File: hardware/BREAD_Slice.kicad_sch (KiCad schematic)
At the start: 15 parts, among them J1 I2C_01x04, J2 Conn_01x10_Female

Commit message: added opamps
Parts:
- removed J1: I2C_01x04, Connector_JST:JST_SH_SM04B-SRSS-TB_1x04-1MP_P1.00mm_Horizontal, symbol SparkFun-Connector:I2C_01x04
- added NT1: NetTie_2, NetTie:NetTie-2_SMD_Pad2.0mm, symbol Device:NetTie_2
- added U2: LM339, symbol Comparator:LM339
- added U3: MCP6242T-E/SN, Package_DFN_QFN:DFN-8-1EP_3x2mm_P0.5mm_EP1.75x1.45mm, symbol Amplifier_Operational:MCP6002-xMC
- added U4: TLC27L2BCDR, Package_SO:SOIC-8_3.9x4.9mm_P1.27mm, symbol Amplifier_Operational:TLC27M2xD
- D1: PROD_ID (none) -> DIO-12503
- HS1: footprint KML-Custom:Thermal Pad -> kml-custom:Thermal Pad
- U1: value ~ -> AP63205
- renumbered J2 to J1
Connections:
- net GND: now also NT1.1; no longer J1.1 (Pin_1), J1.10 (Pin_10), J1.5 (Pin_5)
- net E_STOP renamed ESTOP
- new net: U3.4 (V-), U3.9 (V-)
- new net GNDPWR: J1.1 (Pin_1), J1.10 (Pin_10), J1.5 (Pin_5), NT1.2
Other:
- note added: "5V Switching Supply"
- note added: "Arduino Nano"
- note added: "Backplane Conn."
- note added: "Color Scheme Legend: ---------------------------------------------------------- color - value - reference ---------------------------------------------------------- • Red - red3 - Analog 5V Supply (e.g., for amps, ADC, references) • Brown - orange1 - Analog Ground (sensor/amp/ADC ground) • Orange - orange3 - Digital 5V Supply (MCU, digital circuits) • Black - black - Digital Ground (MCU ground) •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"
- note added: "Mounting Holes"
- note added: "Pinout Details Arduino Nano: -------------------------------------------------------------------------------------------------------------------- Pin | Function | Limitations/Notes -------------------------------------------------------------------------------------------------------------------- VIN | External Supply Input | External power source 7-12V GND | Ground | First GND pin available for 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"
- note added: "RGB LED"
- moved on the sheet: A1, C1, C2, C3, C4, H1, H2, H3, H4, L1, U1

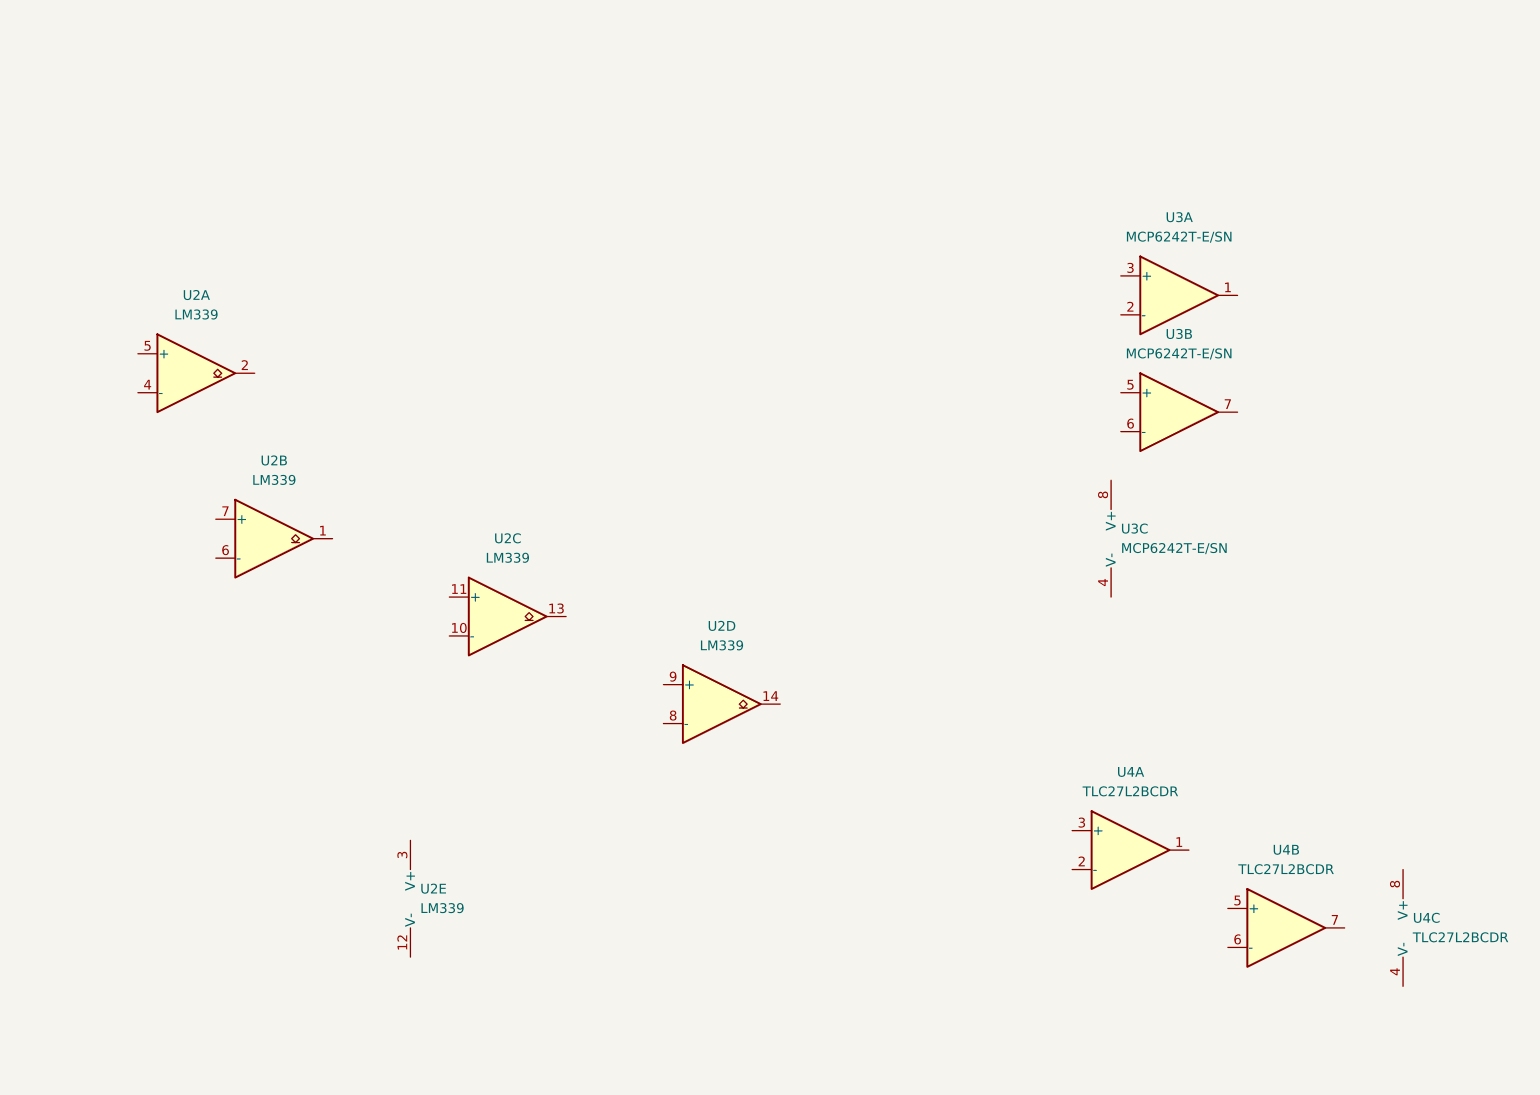
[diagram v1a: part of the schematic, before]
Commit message: completed CC driver for LEDs
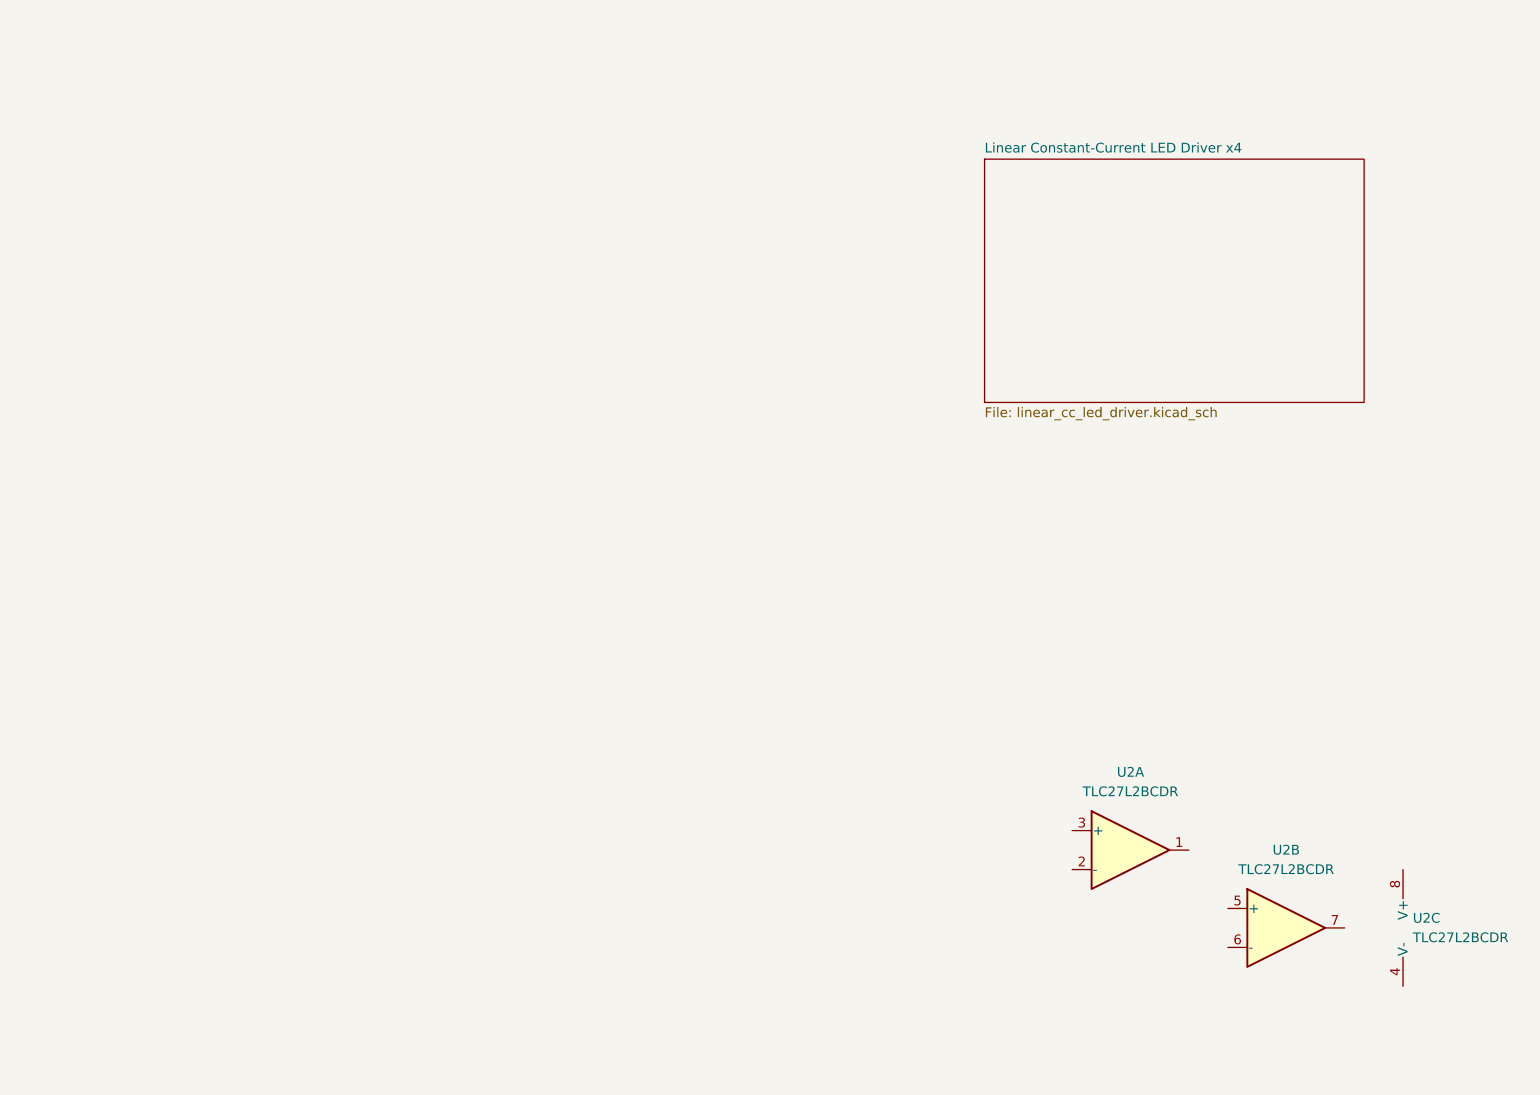
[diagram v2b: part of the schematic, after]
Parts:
- removed U2: LM339, symbol Comparator:LM339
- removed U3: MCP6242T-E/SN, Package_DFN_QFN:DFN-8-1EP_3x2mm_P0.5mm_EP1.75x1.45mm, symbol Amplifier_Operational:MCP6002-xMC
- renumbered U4 to U2
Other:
- added sheet Linear Constant‐Current LED Driver x4 (linear_cc_led_driver.kicad_sch)

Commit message: finalized initial schematic and board
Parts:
- removed U2: TLC27L2BCDR, Package_SO:SOIC-8_3.9x4.9mm_P1.27mm, symbol Amplifier_Operational:TLC27M2xD
- added D2, D3, D4, D5: LED, SparkFun-LED:LED_0603_1608Metric, symbol SparkFun-LED:LED
- added D6, D7: D_Photo, symbol Device:D_Photo_Filled
- added J2, J3, J4, J5, J6, J7: Conn_01x02, Connector_Molex:Molex_PicoBlade_53048-0210_1x02_P1.25mm_Horizontal, symbol Connector_Generic:Conn_01x02
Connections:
- net PWM2: now reaches A1.12 (D9)
- net PWM3: now reaches A1.13 (D10)
- net PWM4: now reaches A1.14 (D11)
- net PD1: now reaches A1.19 (A0)
- net PD2: now reaches A1.20 (A1)
- net PWM1: now reaches A1.9 (D6)
- new net Linear Constant‐Current LED Driver x4/LED_ANODE_1: D2.2 (A), J2.2 (Pin_2)
- new net Linear Constant‐Current LED Driver x4/LED_ANODE_2: D3.2 (A), J3.2 (Pin_2)
- new net Linear Constant‐Current LED Driver x4/LED_ANODE_3: D4.2 (A), J4.2 (Pin_2)
- new net Linear Constant‐Current LED Driver x4/LED_ANODE_4: D5.2 (A), J5.2 (Pin_2)
- new net Linear Constant‐Current LED Driver x4/LED_CATHODE_1: D2.1 (K), J2.1 (Pin_1)
- new net Linear Constant‐Current LED Driver x4/LED_CATHODE_2: D3.1 (K), J3.1 (Pin_1)
- new net Linear Constant‐Current LED Driver x4/LED_CATHODE_3: D4.1 (K), J4.1 (Pin_1)
- new net Linear Constant‐Current LED Driver x4/LED_CATHODE_4: D5.1 (K), J5.1 (Pin_1)
- new net Photodiode TIA Amplifier x2/PD_ANODE1: D6.1 (K), J6.2 (Pin_2)
- new net Photodiode TIA Amplifier x2/PD_ANODE2: D7.1 (K), J7.2 (Pin_2)
- new net Photodiode TIA Amplifier x2/PD_CATHODE1: D6.2 (A), J6.1 (Pin_1)
- new net Photodiode TIA Amplifier x2/PD_CATHODE2: D7.2 (A), J7.1 (Pin_1)
- no-connect marks 22 -> 16
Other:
- added sheet Photodiode TIA Amplifier x2 (pd_amp.kicad_sch)
- added sheet TPS7A4901-VAA (tps7a4901.kicad_sch)
- sheet Linear Constant‐Current LED Driver x4 ports: added +5V, GND, LED_ANODE_1, LED_ANODE_2, LED_ANODE_3, LED_ANODE_4, LED_CATHODE_1, LED_CATHODE_2, LED_CATHODE_3, LED_CATHODE_4, PWM_IN1, PWM_IN2, PWM_IN3, PWM_IN4; removed none
- note added: "Color Scheme Legend: ---------------------------------------------------------- color - value - reference ---------------------------------------------------------- • Red - red3 - Analog 5V Supply • Brown - orange1 - Analog Ground • Orange - orange3 - Digital 5V Supply • Black - black - Ground • Pink - magenta3 - 12V Source Supply (from backplane) • Blue - blue3 - Clock Signals (oscillator, ADC C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"
- note removed: "Color Scheme Legend: ---------------------------------------------------------- color - value - reference ---------------------------------------------------------- • Red - red3 - Analog 5V Supply (e.g., for amps, ADC, references) • Brown - orange1 - Analog Ground (sensor/amp/ADC ground) • Orange - orange3 - Digital 5V Supply (MCU, digital circuits) • Black - black - Digital Ground (MCU ground) •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"
